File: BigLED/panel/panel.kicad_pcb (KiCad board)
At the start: 2 copper layers, 37 parts, among them J1 Power, J2 LED PWR, J3 BTN1, J4 Spkr, J5 BTN2, U1 DAC7311xDCK, U2 LM1085-ADJ, U3 NS4110B_C5334145, U4 IMU, U5 RPi2W

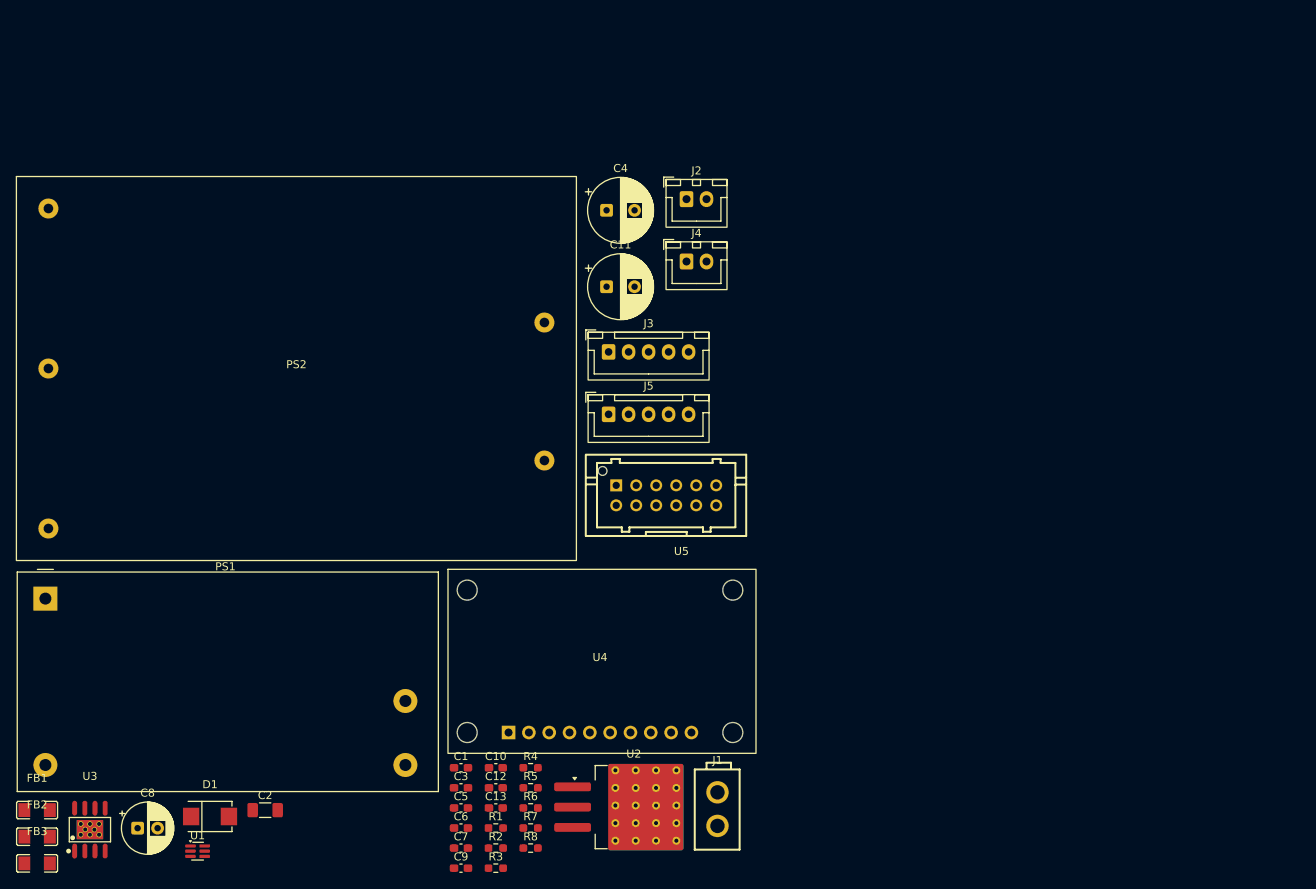
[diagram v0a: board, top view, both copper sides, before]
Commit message: PCB for BigLED Panel started
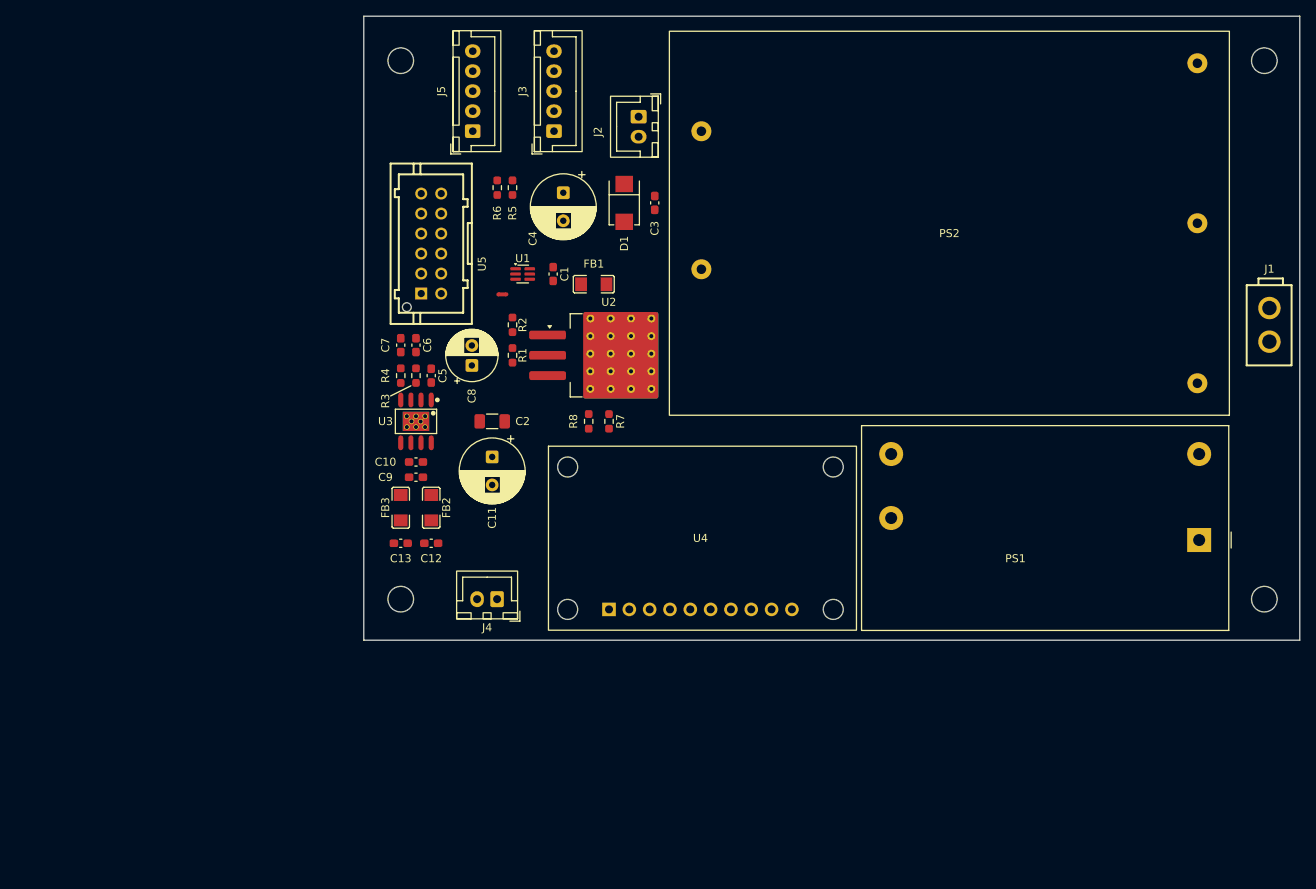
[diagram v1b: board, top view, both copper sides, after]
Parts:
- added H1: MountingHole, MountingHole:MountingHole_3.2mm_M3, F.Cu at (242.6, 35.6)
- added H2: MountingHole, MountingHole:MountingHole_3.2mm_M3, F.Cu at (242.6, 102.9)
- added H3: MountingHole, MountingHole:MountingHole_3.2mm_M3, F.Cu at (134.6, 35.6)
- added H4: MountingHole, MountingHole:MountingHole_3.2mm_M3, F.Cu at (134.6, 102.9)
- added NT1: NetTie_2, NetTie:NetTie-2_SMD_Pad0.5mm, F.Cu at (147.3, 64.8)
- PS1: value IRM-20-12 -> IRM-10-12; footprint Converter_ACDC:Converter_ACDC_MeanWell_IRM-20-xx_THT -> Converter_ACDC:Converter_ACDC_MeanWell_IRM-10-xx_THT
- moved PS1 144.4 mm to (234.4, 95.5), turned to 180 degrees
- moved FB1 95.7 mm to (158.8, 63.5), turned to 180 degrees
- moved D1 92.5 mm to (162.6, 53.3), turned to -90 degrees
- moved J1 91.8 mm to (243.2, 68.6)
- moved PS2 83.6 mm to (203.2, 55.9), turned to 180 degrees
- moved U1 82.8 mm to (149.9, 62.2)
- moved R6 77.6 mm to (146.7, 51.4), turned to -90 degrees
- moved C3 77.0 mm to (166.4, 53.3), turned to -90 degrees
- moved R5 75.1 mm to (148.6, 51.4), turned to -90 degrees
- moved C8 71.3 mm to (143.5, 73.7), turned to 90 degrees
- moved R2 65.4 mm to (148.6, 68.6), turned to 90 degrees
- moved U3 65.3 mm to (136.5, 80.6), turned to 180 degrees
- moved FB2 64.2 mm to (138.4, 91.4), turned to -90 degrees
- moved FB3 63.6 mm to (134.6, 91.4), turned to -90 degrees
- moved C7 63.3 mm to (134.6, 71.1), turned to -90 degrees
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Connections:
- C7 pad 1: GND -> Net-(C7-Pad1)
- PS1 pad 1: Net-(J1-Pin_1) -> Net-(J1-Pin_2)
- PS1 pad 2: Net-(J1-Pin_2) -> Net-(J1-Pin_1)
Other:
- board outline added: 117 x 78 mm

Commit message: Added Simulation for Capacitor voltage drop. Started PCB route for BigLED Pannel
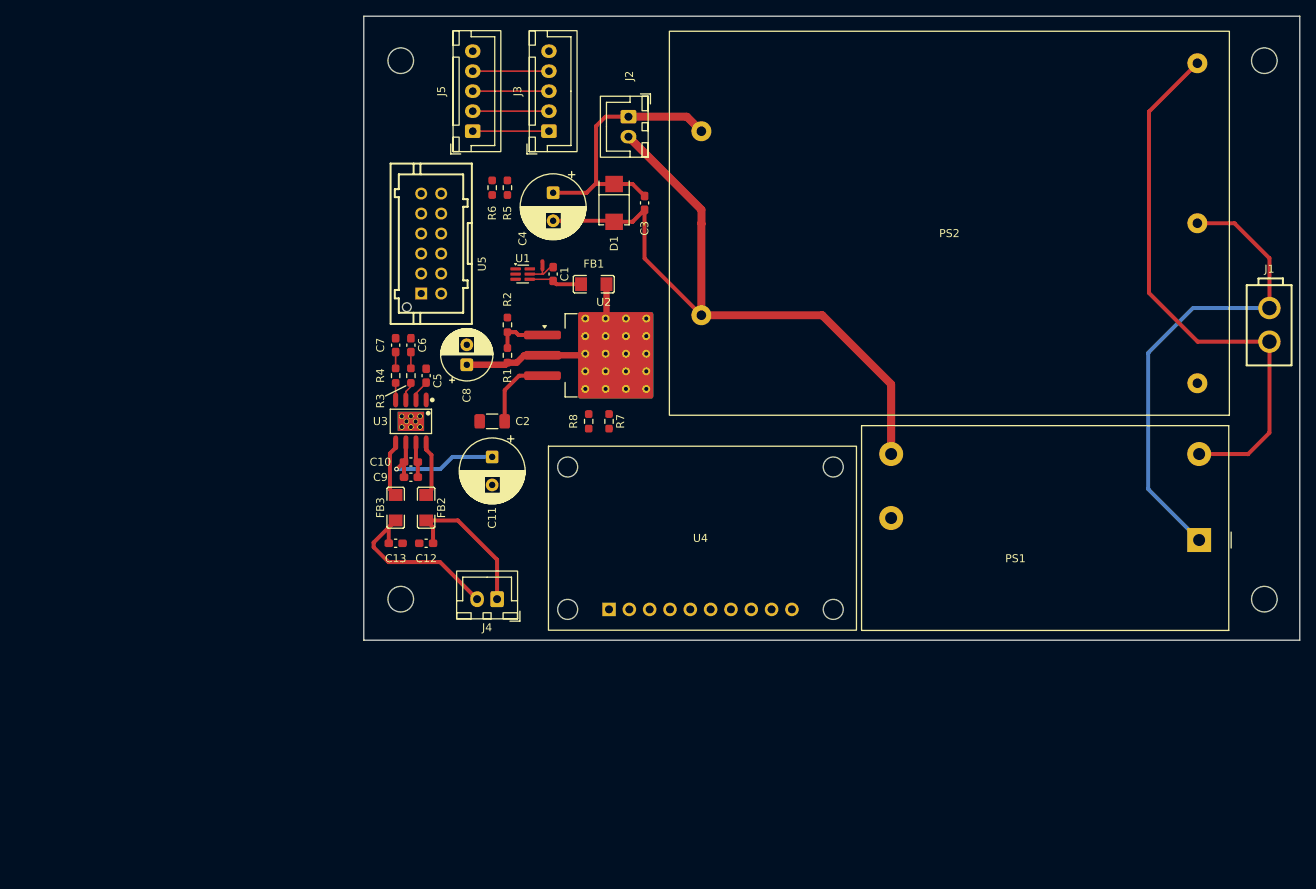
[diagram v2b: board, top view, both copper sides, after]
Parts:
- moved NT1 6.19 mm to (152.3, 61.1), turned to 90 degrees
- moved C3 1.27 mm to (165.1, 53.3)
- moved C4 1.27 mm to (153.7, 52.1)
- moved D1 1.27 mm to (161.3, 53.3)
- moved J2 1.27 mm to (163.1, 42.6)
- moved C8 0.64 mm to (142.9, 73.6)
- moved C10 0.64 mm to (135.9, 85.7)
- moved C12 0.64 mm to (137.8, 95.9)
- moved C5 0.64 mm to (137.8, 74.9)
- moved C6 0.64 mm to (135.9, 71.1)
- moved C9 0.64 mm to (135.9, 87.6)
- moved FB2 0.64 mm to (137.8, 91.4)
- moved R3 0.64 mm to (135.9, 74.9)
- moved U3 0.64 mm to (135.9, 80.6)
- moved C13 0.63 mm to (134.0, 95.9)
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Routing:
- net GND: track 0.00 -> 108.2 mm
- net Net-(J1-Pin_1): track 0.00 -> 70.1 mm
- net Net-(J1-Pin_2): track 0.00 -> 60.6 mm
- net +5V: track 0.00 -> 43.5 mm
- net +3.3V: track 0.00 -> 29.2 mm
- net Net-(J4-Pin_2): track 0.00 -> 23.3 mm
- net Net-(J4-Pin_1): track 0.00 -> 19.0 mm
- net +12V: track 0.00 -> 18.3 mm, vias 0 -> 1
- net SDA: track 0.00 -> 9.53 mm
- net SCL: track 0.00 -> 9.53 mm
- net Net-(U3-VON): track 0.00 -> 7.12 mm
- net Net-(U3-VOP): track 0.00 -> 7.07 mm
- net Net-(U1-AVDD/AVREF): track 0.00 -> 6.67 mm
- net Net-(U2-ADJ): track 0.00 -> 6.52 mm
- net Net-(U3-BYPASS): track 0.00 -> 2.70 mm
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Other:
- rule pad_to_mask_clearance: 0 -> 0.05

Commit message: PCB for BigLED Panel finished
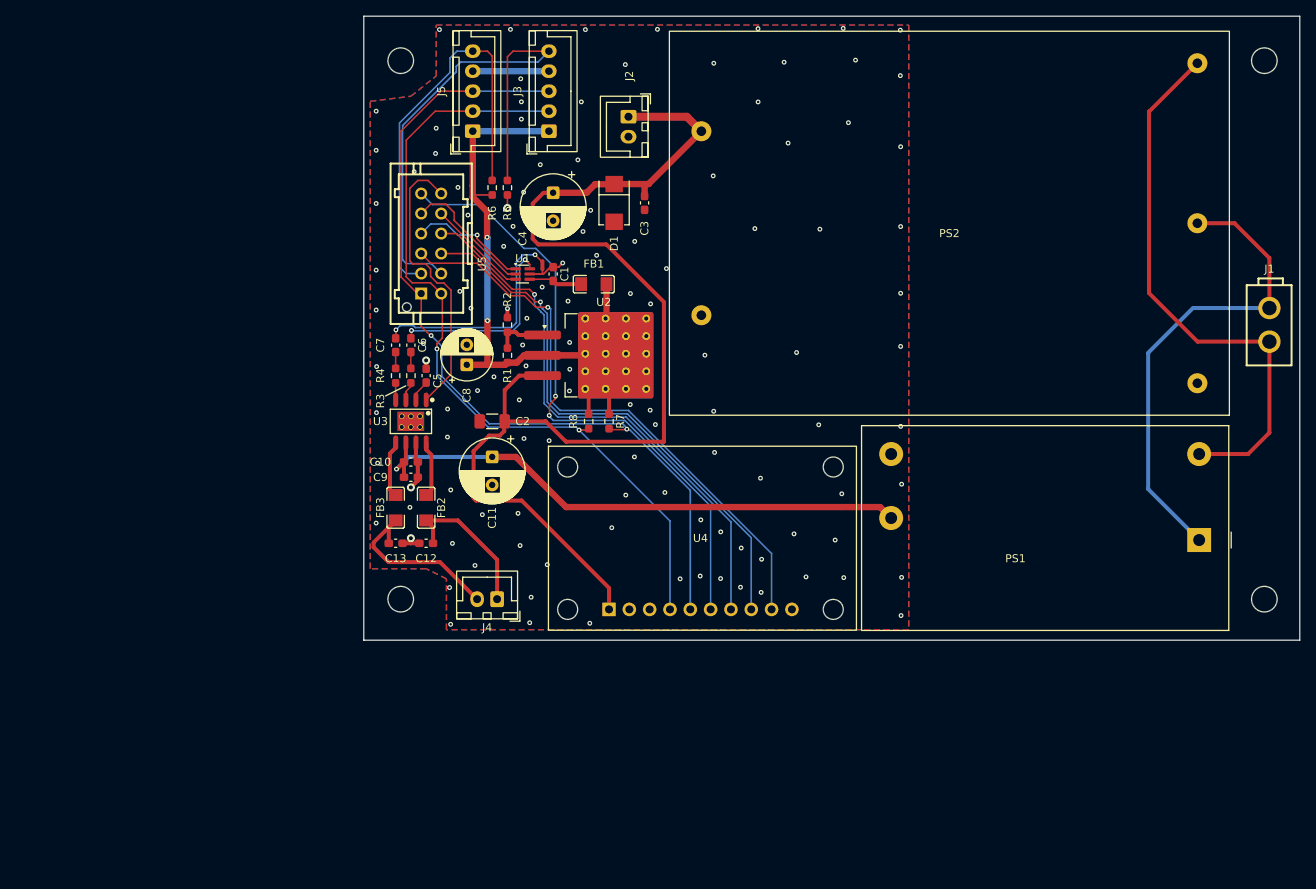
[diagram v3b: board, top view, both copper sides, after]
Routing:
- net +5V: track 43.5 -> 144.3 mm
- net SDA: track 9.53 -> 107.9 mm, vias 0 -> 2
- net SCL: track 9.53 -> 101.3 mm, vias 0 -> 2
- net GND: track 108.2 -> 27.5 mm, vias 0 -> 120
- net Net-(U4-GINT): track 0.00 -> 77.2 mm, vias 0 -> 2
- net Net-(U4-LIN2): track 0.00 -> 73.0 mm, vias 0 -> 1
- net Net-(U4-GRDY): track 0.00 -> 69.4 mm, vias 0 -> 1
- net Net-(U4-LIN1): track 0.00 -> 69.3 mm, vias 0 -> 1
- net Net-(J3-Pin_5): track 0.00 -> 65.8 mm
- net Net-(J5-Pin_5): track 0.00 -> 53.2 mm
- net +12V: track 18.3 -> 71.3 mm
- net +3.3V: track 29.2 -> 73.8 mm, vias 0 -> 2
- net Net-(U3-CTRL): track 0.00 -> 36.3 mm
- net Net-(C7-Pad1): track 0.00 -> 28.3 mm, vias 0 -> 2
- net Net-(U1-VOUT): track 0.00 -> 24.6 mm, vias 0 -> 2
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- added copper zone on B.Cu, net GND
- added copper zone on F.Cu, net GND
